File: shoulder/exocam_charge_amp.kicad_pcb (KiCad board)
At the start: 2 copper layers, 29.6 x 18 mm, 22 parts, among them J1 jstsh8x1, U1 TLV2771CDBVT, U2 TLV2771CDBVT, U3 TLV2771CDBVT

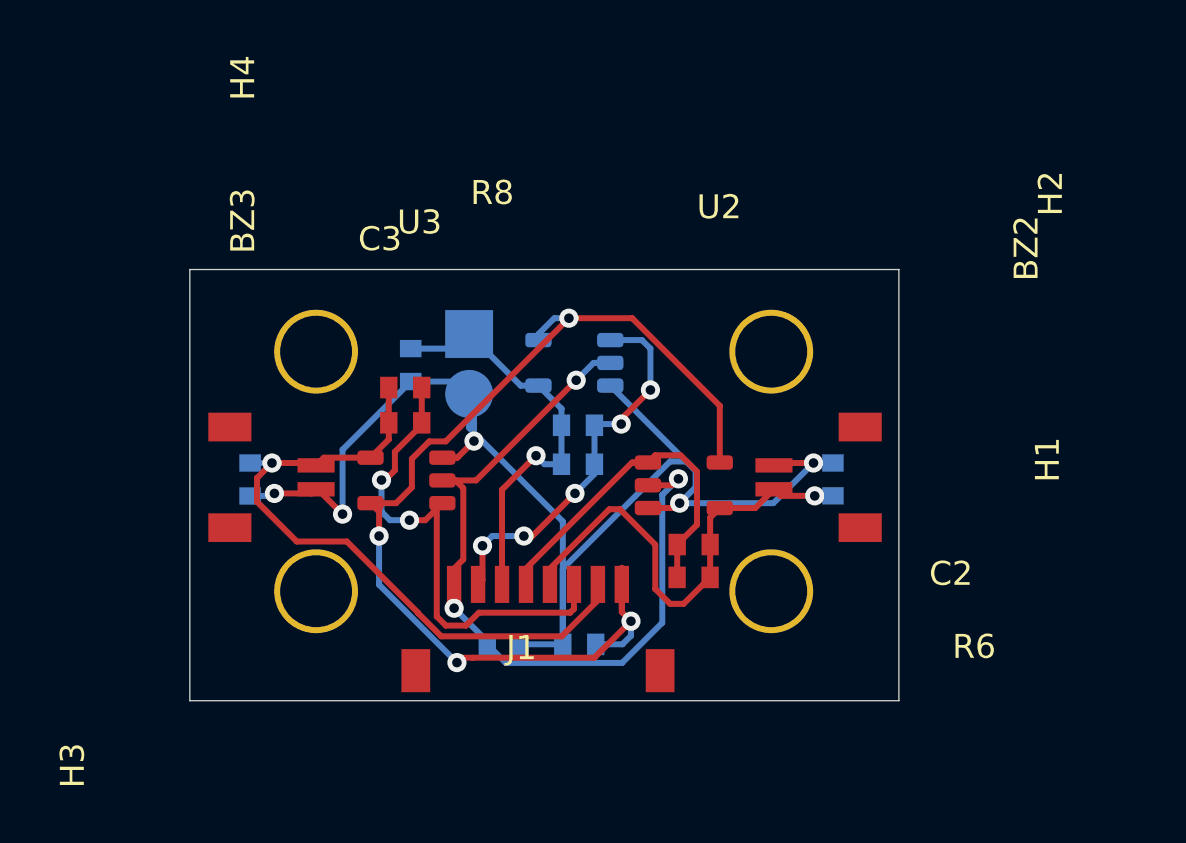
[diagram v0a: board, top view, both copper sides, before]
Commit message: re-did shoulder board to compensate for lack of connectors
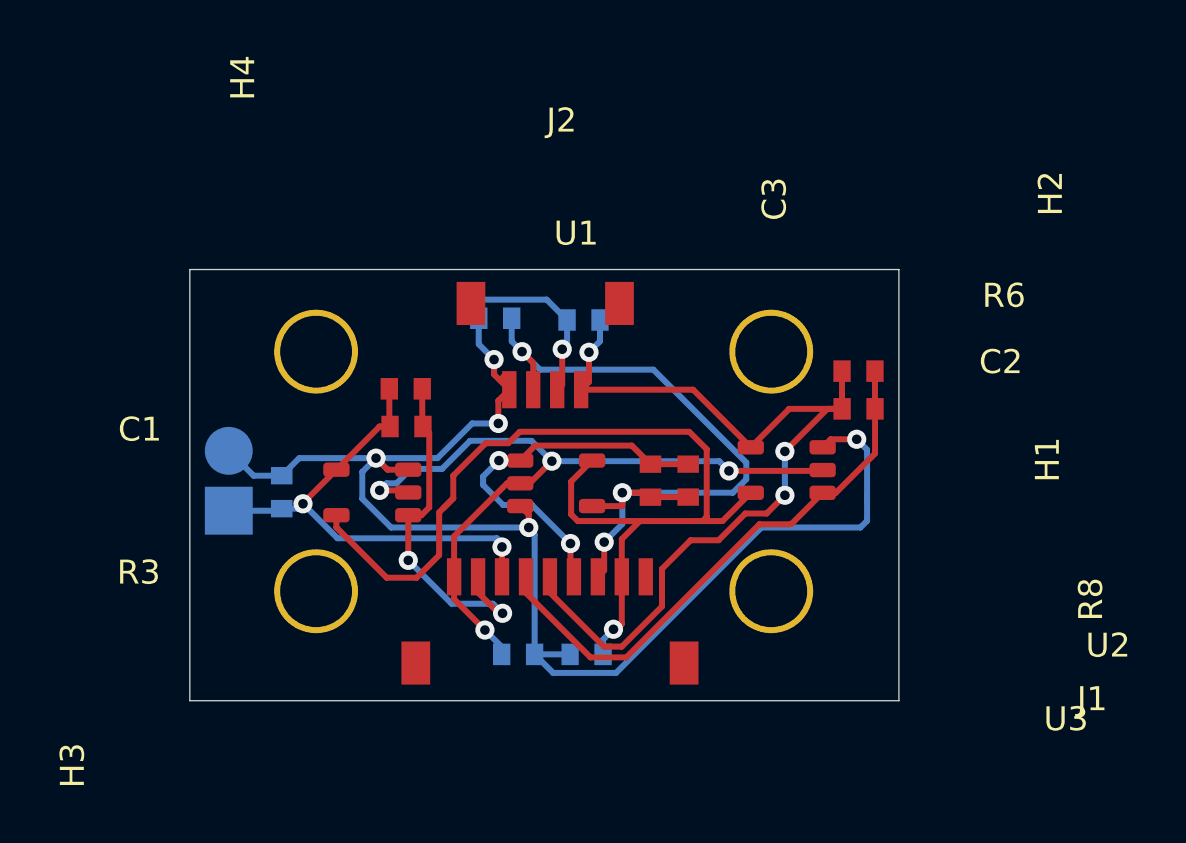
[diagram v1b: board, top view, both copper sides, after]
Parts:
- removed BZ2, BZ3: Buzzer, exocam_charge_amp:jstsh2x1
- added J2: jstsh4x1, exocam_charge_amp:jstsh4x1, F.Cu at (59.4, 63.2)
- C1, R3, U1: moved to F.Cu
- J1: value jstsh8x1 -> jstsh9x1; footprint exocam_charge_amp:jstsh8x1 -> exocam_charge_amp:jstsh9x1
- moved R6 15.9 mm to (74.3, 57.3), turned to 0 degrees
- moved U1 15.0 mm to (53.7, 68.4)
- moved C2 13.4 mm to (74.3, 58.9), turned to 0 degrees
- moved R4 12.3 mm to (47.1, 65.5), turned to 270 degrees
- moved R3 10.9 mm to (55.4, 58.1)
- moved R8 10.5 mm to (64.1, 63.9), turned to 90 degrees
- moved R7 9.03 mm to (59.2, 60.2), turned to 0 degrees
- moved U3 8.98 mm to (60.9, 61.1), turned to 0 degrees
- moved C1 8.75 mm to (55.5, 59.6)
- moved R5 8.67 mm to (62.9, 60.3), turned to 0 degrees
- moved C3 8.35 mm to (62.5, 63.9), turned to 90 degrees
- moved U2 7.93 mm to (71.0, 67.5), turned to 180 degrees
- moved BZ1 6.56 mm to (50.0, 64.2), turned to 90 degrees
- moved R2 0.73 mm to (59.0, 69.2)
- moved R1 0.52 mm to (61.8, 69.2)
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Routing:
- net UNAMP2: track 19.8 -> 37.4 mm, vias 1 -> 3
- net AMP2: track 15.3 -> 24.0 mm
- net VGND: track 59.7 -> 67.3 mm, vias 5 -> 6
- net AMP3: track 21.5 -> 15.9 mm
- net +3V3: track 46.1 -> 42.0 mm, vias 4 -> 1
- net UNAMP1: track 17.3 -> 20.3 mm, vias 1 -> 2
- net AMP1: track 16.4 -> 14.9 mm, vias 5 -> 2
- net UNAMP3: track 28.2 -> 29.3 mm, vias 1 -> 3
- net GND: track 33.4 -> 32.4 mm, vias 3 -> 4

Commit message: added more to the mainboard/daugher board
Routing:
- net GND: track 32.4 -> 33.2 mm
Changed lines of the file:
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@@
     (35 F.Paste user)
     (36 B.SilkS user hide)
-    (37 F.SilkS user)
+    (37 F.SilkS user hide)
     (38 B.Mask user)
     (39 F.Mask user)
@@
   (segment (start 60.1825 59.5221) (end 60.1825 60.6425) (width 0.25) (layer F.Cu) (net 4))
   (segment (start 59.7154 59.055) (end 60.1825 59.5221) (width 0.25) (layer F.Cu) (net 4))
-  (segment (start 62.6392 65.5016) (end 63.9014 65.5016) (width 0.25) (layer F.Cu) (net 4))
-  (segment (start 63.9014 65.5016) (end 63.9014 64.9428) (width 0.25) (layer F.Cu) (net 4))
   (segment (start 63.9014 64.9428) (end 63.9014 64.9428) (width 0.25) (layer F.Cu) (net 4))
   (via (at 63.9014 64.9428) (size 0.8) (drill 0.4) (layers F.Cu B.Cu) (net 4))
@@
   (segment (start 63.1444 68.1886) (end 62.88 68.453) (width 0.25) (layer F.Cu) (net 4))
   (segment (start 63.1444 67.0052) (end 63.1444 68.1886) (width 0.25) (layer F.Cu) (net 4))
+  (segment (start 63.3426 65.5016) (end 63.9014 64.9428) (width 0.25) (layer F.Cu) (net 4))
+  (segment (start 62.6392 65.5016) (end 63.3426 65.5016) (width 0.25) (layer F.Cu) (net 4))
   (segment (start 55.5498 62.1504) (end 55.5786 62.1792) (width 0.25) (layer F.Cu) (net 5))
   (segment (start 55.5498 60.6044) (end 55.5498 62.1504) (width 0.25) (layer F.Cu) (net 5))
@@
   (segment (start 56.88 69.3895) (end 56.88 68.453) (width 0.25) (layer F.Cu) (net 10))
   (segment (start 58.166 70.6755) (end 56.88 69.3895) (width 0.25) (layer F.Cu) (net 10))
-  (via (at 60.96 63.627) (size 0.8) (drill 0.4) (layers F.Cu B.Cu) (net 10))
   (via (at 68.3514 64.0334) (size 0.8) (drill 0.4) (layers F.Cu B.Cu) (net 10))
   (segment (start 72.202 64.0588) (end 72.263 63.9978) (width 0.25) (layer F.Cu) (net 10))
@@
   (segment (start 54.8792 64.8462) (end 54.9656 64.9326) (width 0.25) (layer F.Cu) (net 10))
   (segment (start 53.7718 64.8462) (end 54.8792 64.8462) (width 0.25) (layer F.Cu) (net 10))
-  (segment (start 53.7718 64.8462) (end 54.0664 64.5516) (width 0.25) (layer B.Cu) (net 10))
-  (segment (start 60.0354 64.5516) (end 60.96 63.627) (width 0.25) (layer F.Cu) (net 10))
   (segment (start 59.6392 64.5516) (end 60.0354 64.5516) (width 0.25) (layer F.Cu) (net 10))
   (segment (start 67.945 63.627) (end 68.3514 64.0334) (width 0.25) (layer B.Cu) (net 10))
@@
   (segment (start 72.2274 64.0334) (end 72.263 63.9978) (width 0.25) (layer F.Cu) (net 10))
   (segment (start 68.3514 64.0334) (end 72.2274 64.0334) (width 0.25) (layer F.Cu) (net 10))
-  (segment (start 55.07439 63.95001) (end 56.371201 63.950009) (width 0.25) (layer B.Cu) (net 10))
-  (segment (start 54.4728 64.5516) (end 55.07439 63.95001) (width 0.25) (layer B.Cu) (net 10))
-  (segment (start 54.0664 64.5516) (end 54.4728 64.5516) (width 0.25) (layer B.Cu) (net 10))
   (segment (start 60.110201 62.777201) (end 60.96 63.627) (width 0.25) (layer B.Cu) (net 10))
-  (segment (start 57.544009 62.777201) (end 60.110201 62.777201) (width 0.25) (layer B.Cu) (net 10))
-  (segment (start 56.371201 63.950009) (end 57.544009 62.777201) (width 0.25) (layer B.Cu) (net 10))
+  (segment (start 55.653602 64.8462) (end 57.722601 62.777201) (width 0.25) (layer B.Cu) (net 10))
+  (segment (start 53.7718 64.8462) (end 55.653602 64.8462) (width 0.25) (layer B.Cu) (net 10))
+  (segment (start 57.722601 62.777201) (end 60.110201 62.777201) (width 0.25) (layer B.Cu) (net 10))
+  (segment (start 59.6392 64.5516) (end 60.706 64.4906) (width 0.25) (layer F.Cu) (net 10))
+  (segment (start 60.706 64.4906) (end 60.645 64.5516) (width 0.25) (layer F.Cu) (net 10))
+  (via (at 60.706 64.4906) (size 0.8) (drill 0.4) (layers F.Cu B.Cu) (net 10))
+  (segment (start 60.706 63.881) (end 60.96 63.627) (width 0.25) (layer B.Cu) (net 10))
+  (segment (start 60.706 64.4906) (end 60.706 63.881) (width 0.25) (layer B.Cu) (net 10))
 )

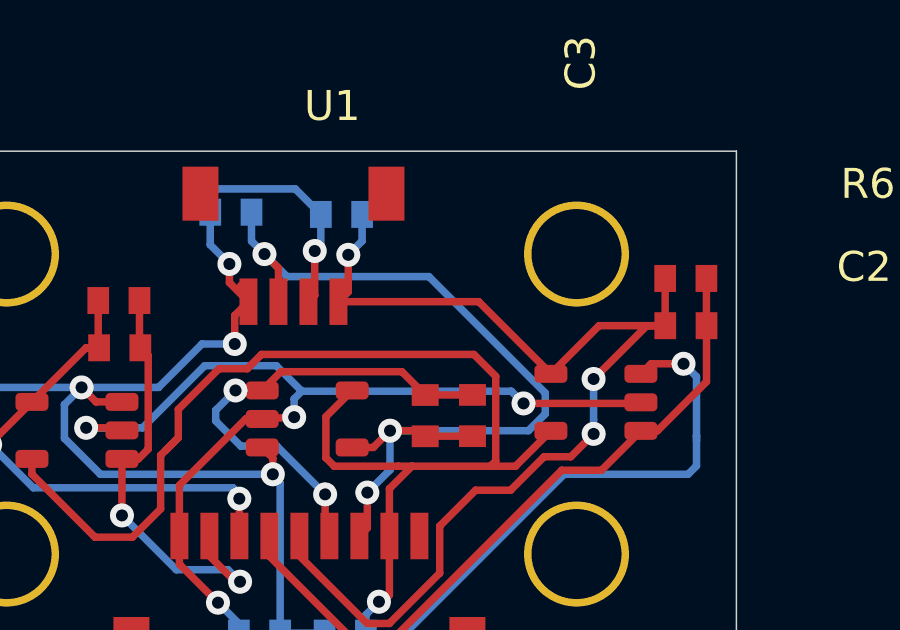
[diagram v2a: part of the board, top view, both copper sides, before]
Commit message: re added teensy footprints
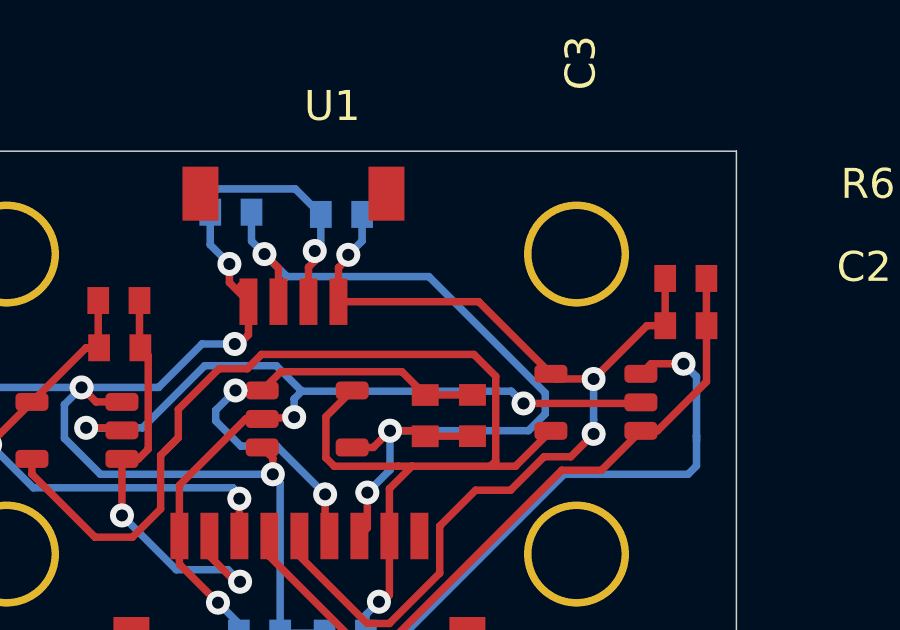
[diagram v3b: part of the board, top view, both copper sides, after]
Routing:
- net UNAMP2: track 37.4 -> 34.5 mm
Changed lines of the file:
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@@
     (thickness 1.6)
     (drawings 4)
-    (tracks 239)
+    (tracks 242)
     (zones 0)
     (modules 21)
@@
       (effects (font (size 1 1) (thickness 0.15)))
     )
+    (fp_line (start 2.185 3) (end 2.185 6.84) (layer Dwgs.User) (width 0.12))
+    (fp_line (start 2.185 3) (end -4.805 3) (layer Dwgs.User) (width 0.12))
+    (fp_line (start -4.805 6.84) (end -4.805 3) (layer Dwgs.User) (width 0.12))
     (fp_line (start -4.805 6.84) (end 2.185 6.84) (layer Dwgs.User) (width 0.12))
-    (fp_line (start -4.805 6.84) (end -4.805 3) (layer Dwgs.User) (width 0.12))
-    (fp_line (start 2.185 3) (end -4.805 3) (layer Dwgs.User) (width 0.12))
-    (fp_line (start 2.185 3) (end 2.185 6.84) (layer Dwgs.User) (width 0.12))
     (pad 5 smd rect (at -4.41 6.14 180) (size 1.2 1.8) (layers F.Cu F.Paste F.Mask)
       (net 12 "Net-(J2-Pad5)"))
@@
       (effects (font (size 1 1) (thickness 0.15)))
     )
+    (fp_line (start 7.185 3) (end 7.185 6.84) (layer Dwgs.User) (width 0.12))
+    (fp_line (start -4.805 3) (end 7.185 3) (layer Dwgs.User) (width 0.12))
+    (fp_line (start -4.805 6.84) (end -4.805 3) (layer Dwgs.User) (width 0.12))
     (fp_line (start -4.805 6.84) (end 7.185 6.84) (layer Dwgs.User) (width 0.12))
-    (fp_line (start -4.805 6.84) (end -4.805 3) (layer Dwgs.User) (width 0.12))
-    (fp_line (start -4.805 3) (end 7.185 3) (layer Dwgs.User) (width 0.12))
-    (fp_line (start 7.185 3) (end 7.185 6.84) (layer Dwgs.User) (width 0.12))
     (pad 9 smd rect (at 5.19 2.54) (size 0.6 1.55) (layers F.Cu F.Paste F.Mask)
       (net 8 "Net-(J1-Pad9)"))
@@
   (segment (start 58.7248 62.0522) (end 58.7248 62.0014) (width 0.25) (layer B.Cu) (net 1))
   (via (at 58.7248 62.0522) (size 0.8) (drill 0.4) (layers F.Cu B.Cu) (net 1))
-  (segment (start 58.7248 61.1002) (end 59.1825 60.6425) (width 0.25) (layer F.Cu) (net 1))
-  (segment (start 58.7248 62.0522) (end 58.7248 61.1002) (width 0.25) (layer F.Cu) (net 1))
   (segment (start 59.1825 60.3499) (end 58.929 60.0964) (width 0.25) (layer F.Cu) (net 1))
   (segment (start 59.1825 60.6425) (end 59.1825 60.3499) (width 0.25) (layer F.Cu) (net 1))
@@
   (segment (start 61.3918 58.9534) (end 61.3918 58.9534) (width 0.25) (layer B.Cu) (net 1))
   (via (at 61.3918 58.9534) (size 0.8) (drill 0.4) (layers F.Cu B.Cu) (net 1))
-  (segment (start 61.3918 60.4332) (end 61.1825 60.6425) (width 0.25) (layer F.Cu) (net 1))
-  (segment (start 61.3918 58.9534) (end 61.3918 60.4332) (width 0.25) (layer F.Cu) (net 1))
   (segment (start 60.743799 56.882999) (end 61.595 57.7342) (width 0.25) (layer B.Cu) (net 1))
   (segment (start 57.983601 56.882999) (end 60.743799 56.882999) (width 0.25) (layer B.Cu) (net 1))
@@
   (segment (start 60.2395 71.6915) (end 61.014501 72.466501) (width 0.25) (layer B.Cu) (net 1))
   (segment (start 53.6194 63.5) (end 56.1848 63.5) (width 0.25) (layer B.Cu) (net 1))
+  (segment (start 56.1848 63.5) (end 57.6326 62.0522) (width 0.25) (layer B.Cu) (net 1))
   (segment (start 57.6326 62.0522) (end 58.7248 62.0522) (width 0.25) (layer B.Cu) (net 1))
-  (segment (start 56.1848 63.5) (end 57.6326 62.0522) (width 0.25) (layer B.Cu) (net 1))
+  (segment (start 58.7248 62.0522) (end 58.8772 62.0522) (width 0.25) (layer F.Cu) (net 1))
+  (segment (start 59.1825 61.7469) (end 59.1825 60.6425) (width 0.25) (layer F.Cu) (net 1))
+  (segment (start 58.8772 62.0522) (end 59.1825 61.7469) (width 0.25) (layer F.Cu) (net 1))
+  (segment (start 61.3918 58.9534) (end 61.3918 59.2836) (width 0.25) (layer F.Cu) (net 1))
+  (segment (start 61.1825 59.4929) (end 61.1825 60.6425) (width 0.25) (layer F.Cu) (net 1))
+  (segment (start 61.3918 59.2836) (end 61.1825 59.4929) (width 0.25) (layer F.Cu) (net 1))
   (segment (start 49.6824 65.6082) (end 50.3682 65.6082) (width 0.25) (layer B.Cu) (net 2))
   (segment (start 50.3682 65.6082) (end 50.5714 65.405) (width 0.25) (layer B.Cu) (net 2))
@@
   (segment (start 73.0724 61.4392) (end 73.0758 61.4426) (width 0.25) (layer F.Cu) (net 3))
   (segment (start 73.0724 59.8678) (end 73.0724 61.4392) (width 0.25) (layer F.Cu) (net 3))
-  (segment (start 70.8682 61.4426) (end 69.263 63.0478) (width 0.25) (layer F.Cu) (net 3))
-  (segment (start 73.0758 61.4426) (end 70.8682 61.4426) (width 0.25) (layer F.Cu) (net 3))
   (segment (start 66.8577 60.6425) (end 69.263 63.0478) (width 0.25) (layer F.Cu) (net 3))
   (segment (start 62.1825 60.6425) (end 66.8577 60.6425) (width 0.25) (layer F.Cu) (net 3))
@@
   (segment (start 62.5094 59.0804) (end 62.5094 59.0804) (width 0.25) (layer B.Cu) (net 3))
   (via (at 62.5094 59.0804) (size 0.8) (drill 0.4) (layers F.Cu B.Cu) (net 3))
-  (segment (start 62.5094 60.3156) (end 62.1825 60.6425) (width 0.25) (layer F.Cu) (net 3))
-  (segment (start 62.5094 59.0804) (end 62.5094 60.3156) (width 0.25) (layer F.Cu) (net 3))
   (segment (start 72.4633 61.4426) (end 70.68675 63.21915) (width 0.25) (layer F.Cu) (net 3))
   (segment (start 73.0758 61.4426) (end 72.4633 61.4426) (width 0.25) (layer F.Cu) (net 3))
@@
   (segment (start 65.5574 69.691102) (end 63.879751 71.368751) (width 0.25) (layer F.Cu) (net 3))
   (segment (start 65.5574 68.1228) (end 65.5574 69.691102) (width 0.25) (layer F.Cu) (net 3))
+  (segment (start 69.43435 63.21915) (end 69.263 63.0478) (width 0.25) (layer F.Cu) (net 3))
+  (segment (start 70.68675 63.21915) (end 69.43435 63.21915) (width 0.25) (layer F.Cu) (net 3))
+  (segment (start 62.5094 59.0804) (end 62.5094 59.182) (width 0.25) (layer F.Cu) (net 3))
+  (segment (start 62.1825 59.5089) (end 62.1825 60.6425) (width 0.25) (layer F.Cu) (net 3))
+  (segment (start 62.5094 59.182) (end 62.1825 59.5089) (width 0.25) (layer F.Cu) (net 3))
   (segment (start 65.0782 65.1256) (end 65.0748 65.129) (width 0.25) (layer F.Cu) (net 4))
   (segment (start 66.6496 65.1256) (end 65.0782 65.1256) (width 0.25) (layer F.Cu) (net 4))
